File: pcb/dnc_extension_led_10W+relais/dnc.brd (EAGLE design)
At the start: 97.2 x 88 mm, 132 parts, among them IC1 LM2596S, IC2 74S244DW, Q1 IRF9321PBF, Q10 BSS316, Q11 BSS316, Q12 BSS138, Q13 BSS138, Q2 BSS670, Q3 BSS138, Q4 BSS670, Q5 BSS138, Q6 BSS670, Q7 BSS138, Q8 BSS138, Q9 BSS670, U1 MAX202CDWR, U2 74HCT595D, U3 TC7SU04F, U4 AL8807, U5 AL8807, U6 TC7SU04F

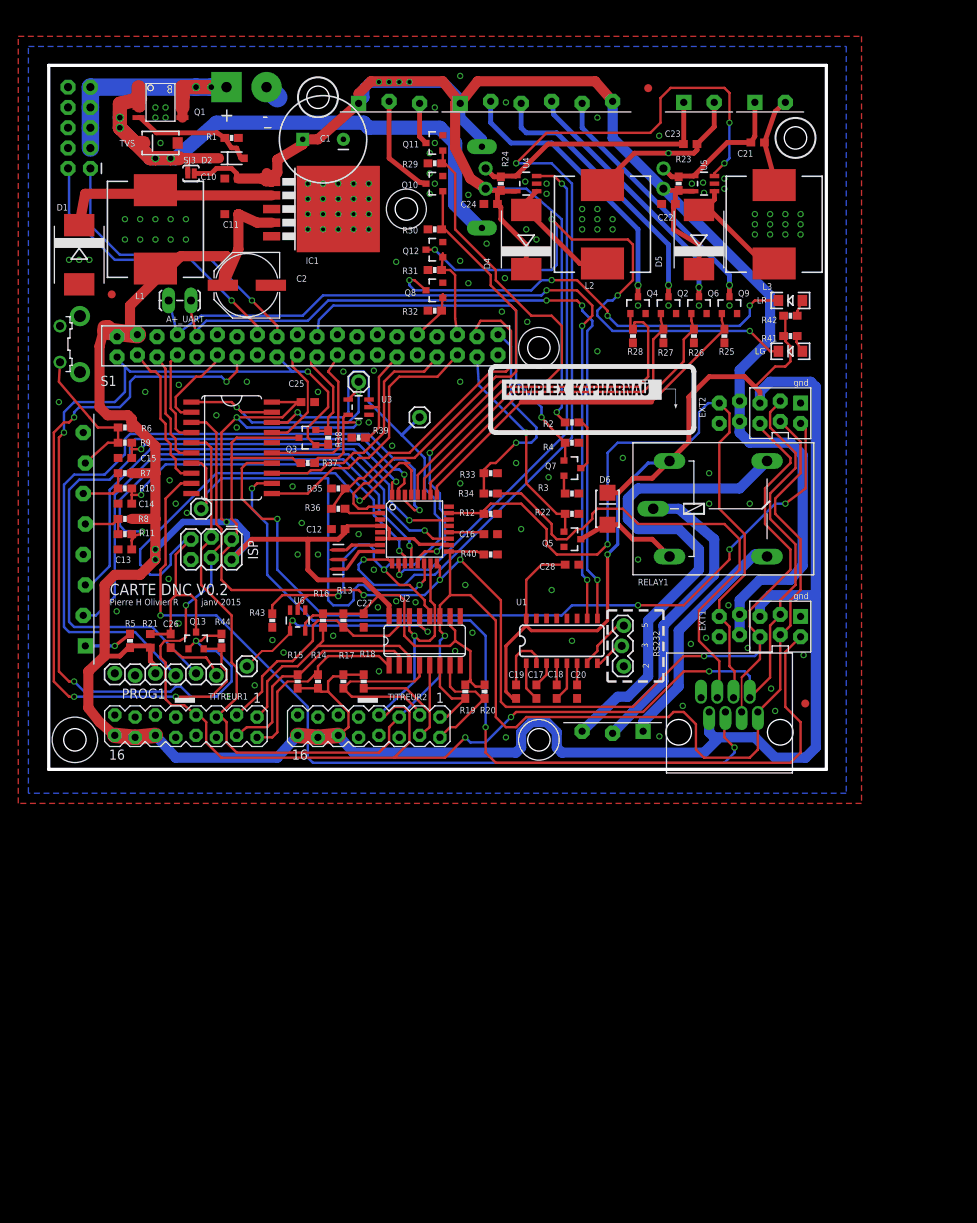
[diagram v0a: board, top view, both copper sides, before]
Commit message: add remote + enclosure
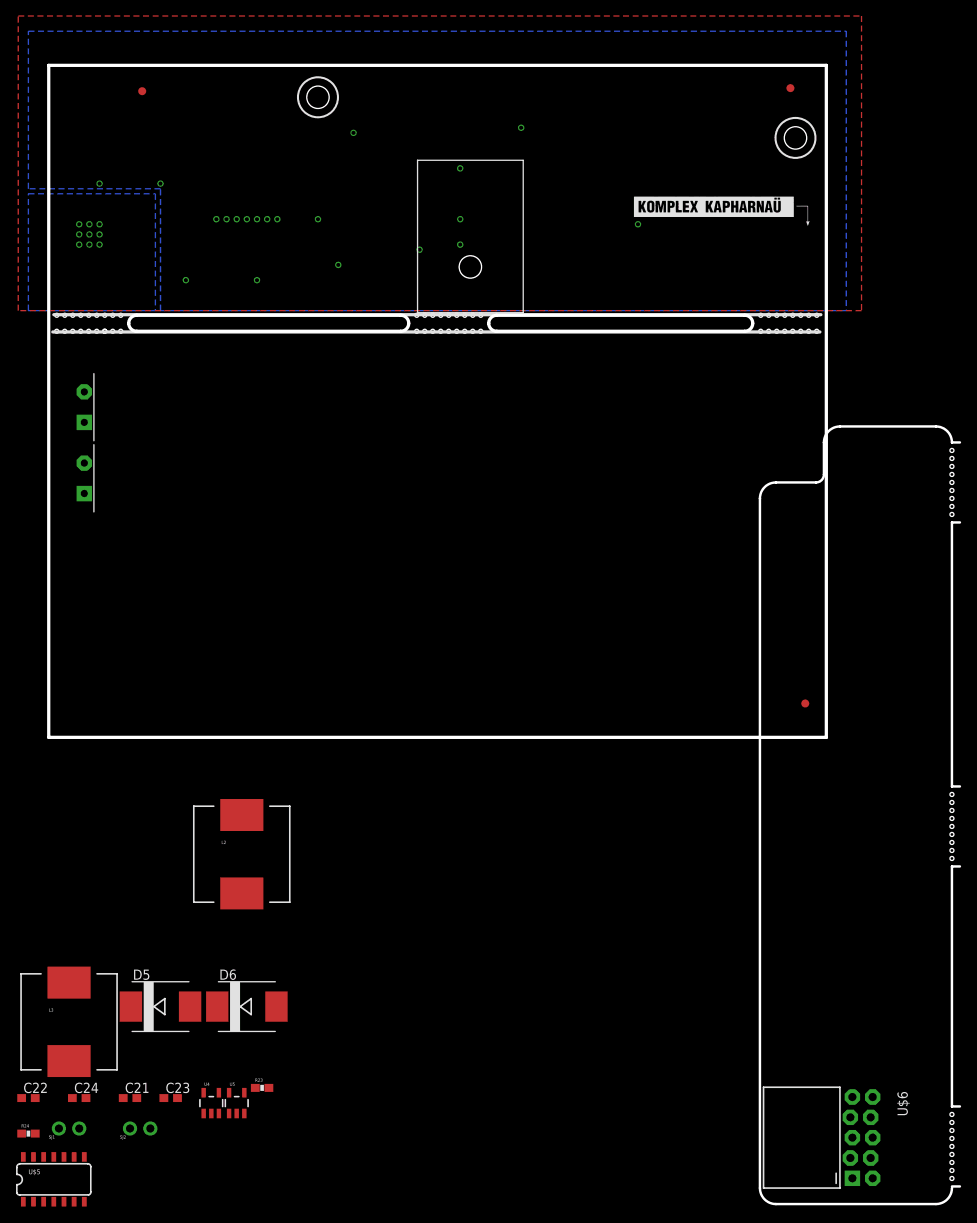
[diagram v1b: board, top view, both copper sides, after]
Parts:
- removed 16MHZ: 16MHZ, SparkFun-FreqCtrl:RESONATOR-SMD
- removed A+_UART: (no value), SparkFun:1X02_LOCK_LONGPADS
- removed AT328: ATMEGA328, SparkFun:TQFP32-08
- removed C1: 680uF30mm, SparkFun:CPOL-RADIAL-1000UF-25V
- removed C10, C11, C12, C16, C17, C18, C19, C20, C25, C26, C27, C28: 0.1uF, rcl:C0603
- removed C13, C14, C15: 1uF, rcl:C0603
- removed C2: 220u, rcl:PANASONIC_E
- removed D1, D4: 40v5A, diode:SMC
- removed D2: 10V, SparkFun-DiscreteSemi:SOD-123
- removed EXT1: EXT1, pierre_vv:EXTPINDNC
- removed EXT2: EXT2, pierre_vv:EXTPINDNC
- removed F1: 8A, SparkFun:PTC
- removed IC1: LM2596S, national-semiconductor:TO263-5
- removed IC2: 74S244DW, 74xx-us:SO20W
- removed ISP: AVR_SPI_PRG_62X3_LOCK, SparkFun:2X3_LOCK
- removed JP1: CHARGEUR, SparkFun:2X5-SHROUDED_LOCK
- removed JP2: regrck, SparkFun-Connectors:1X01
- removed JP3: atmega cs, SparkFun-Connectors:1X01
- removed JP4: allcs, SparkFun-Connectors:1X01
- removed JP5: OE 595, SparkFun-Connectors:1X01
- removed L1: 68nH3A, SparkFun:CDRH125
- removed LG, LR: (no value), SparkFun-LED:LED-1206
- removed PLUG_3.81_1: FLEX, pierre_vv:PLUG_03
- removed PLUG_3.81_2: RELAY, pierre_vv:PLUG_03
- removed PLUG_3.81_2_1: LED10W2, pierre_vv:PLUG_02
- removed PLUG_3.81_6_1: GYRO LED, pierre_vv:PLUG_06
- removed PROG1: (no value), SparkFun:1X06_LOCK
- removed Q1: IRF9321PBF, pierre_vv:SO-8
- removed Q10, Q11: BSS316, SparkFun-DiscreteSemi:SOT23-3
- removed Q12, Q13, Q3, Q5, Q7, Q8: BSS138, SparkFun-DiscreteSemi:SOT23-3
- removed Q2, Q4, Q6, Q9: BSS670, SparkFun-DiscreteSemi:SOT23-3
- removed R1, R13, R14, R15, R16, R17, R18, R19, R20, R22, R25, R26, R27, R28, R29, R30, R31, R32, R4: 100K, SparkFun-Passives:0603-RES
- removed R10, R11, R9: 33K, SparkFun-Passives:0603-RES
- removed R12: (no value), SparkFun-Passives:0603-RES
- removed R2: 100k1%, SparkFun-Passives:0603-RES
- removed R21: 10K, rcl:R0603
- removed R3: 10k1%, SparkFun-Passives:0603-RES
- removed R33, R35: 20K, SparkFun-Passives:0603-RES
- removed R34, R36, R37, R38, R39, R40, R43, R44: 10K, SparkFun-Passives:0603-RES
- removed R41, R42, R5: 1K, SparkFun-Passives:0603-RES
- removed R6, R7, R8: 56K, SparkFun-Passives:0603-RES
- removed RAW_IN: DNC_IN2PWR, pierre_vv:DNC_IN2_PWR
- removed RELAY1: G5L, relay:G5LE
- removed RS232: (no value), SparkFun-Connectors:1X03_LOCK
- removed S1: (no value), switch-omron:B3F-31XX
- removed SJ3: JUMPER-PAD-2-NC_BY_PASTE, SparkFun-Passives:PAD-JUMPER-2-NC_BY_PASTE_YES_SILK
- removed TITREUR1, TITREUR2: DNC_TITREUR, pierre_vv:DNC_TITREUR
- removed TVS: TVS-30V, SparkFun:SMA-DIODE
- removed U$4: RASPIA+, pierre_vv:RASPIA+
- removed U$8: RJ45-EXTDNC, con-amphenol-rj45-ld:RJ45-TRAFO
- removed U1: MAX202CDWR, SparkFun-DigitalIC:SO016
- removed U2: 74HCT595D, IC:SO16
- removed U3, U6: TC7SU04F, SparkFun-DigitalIC:SOT23-5
- added PLUG_3.81_2_3: LED10W1, pierre_vv:PLUG_02
- added U$5: ATTINY84, SparkFun-DigitalIC:SO14
- D6: value (none) -> 40v5A; device SparkFun-DiscreteSemi:SMA-DIODE_ALT -> diode:SMC
- PLUG_3.81_2_2: value LED10W1 -> LED10W2
- U$6: value M08 -> (none); device pierre_vv:PLUG_08 -> pierre_vv:2X5_RIGHTANGLEDNC
- moved C21 142.9 mm to (10.2, -45.1)
- moved C22 137.4 mm to (-2.54, -45.1), turned to 0 degrees
- moved C23 135.8 mm to (15.2, -45.1)
- moved SJ2 135.6 mm to (11.4, -48.9), turned to 0 degrees
- moved L3 133.1 mm to (2.54, -35.6), turned to 0 degrees
- moved R24 132.6 mm to (-2.54, -49.5), turned to 0 degrees
- moved SJ1 129.7 mm to (2.54, -48.9), turned to 0 degrees
- moved U5 128.9 mm to (23.5, -45.7), turned to 0 degrees
- moved R23 124.4 mm to (26.7, -43.8), turned to 0 degrees
- moved C24 123.0 mm to (3.81, -45.1), turned to 0 degrees
- moved U4 121.5 mm to (20.3, -45.7), turned to 0 degrees
- moved D5 117.2 mm to (14.0, -33.7), turned to 0 degrees
- moved PLUG_3.81_2_2 97.8 mm to (4.45, 32.4), turned to 90 degrees
- moved L2 90.7 mm to (24.1, -14.6), turned to 0 degrees
- moved U$6 85.6 mm to (88.9, 38.9), turned to 270 degrees
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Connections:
- removed net +3V3: Q13.1, Q3.1, R38.2, R44.2, U$4.1, U$4.17
- removed net +5V: AT328.18, AT328.4, AT328.6, C11.1, C12.1, C19.1, C2.+, C25.1, C27.1, C28.1, D6.C, EXT1.5V, EXT2.5V, IC1.4, IC2.20, ISP.2, L1.2, PROG1.4, R13.2, R14.2, R15.2, R16.2, R17.2, R18.2, R19.2, R20.2, R21.2, R37.2, R41.2, R42.2, R5.2, R6.2, R7.2, R8.2, RELAY1.2, TITREUR1.12, TITREUR1.14, TITREUR1.16, TITREUR2.12, TITREUR2.14, TITREUR2.16, U$4.2, U$4.4, U$8.1, U1.16, U2.10, U2.16, U3.5, U6.5
- removed net /REG_RCK_5V=ACTIVE_CS: JP5.1, U2.13, U6.4
- removed net ALL_CS_ENABLE_ACTIVE_LOW_5V: IC2.1, IC2.19, JP4.1, U3.4
- removed net ANALOG_BAT: AT328.24
- removed net ANALOG_RAW: Q7.2, R3.2
- removed net AREF: AT328.20, C16.1
- removed net ATMEGA_CS: IC2.13, U$4.33
- removed net ATMEGA_CS_5V: AT328.14, IC2.7, JP3.1
- removed net CHARGING: JP1.2, U$4.16
- removed net CODE: AT328.23, EXT1.RETOURANALOG, EXT2.RETOURANALOG, R12.1, U$8.6
- removed net CS_TRIGGER_ACTIVE_HIGH: R39.2, U$4.29, U3.2
- removed net DTR: C26.1, PROG1.1
- removed net EXT1_CS: IC2.8, U$4.3
- removed net EXT1_CS_5V: EXT1./CS, IC2.12
- removed net EXT2_CS: IC2.6, U$4.5
- removed net EXT2_CS_5V: EXT2./CS, IC2.14
- removed net EXT3_CS: IC2.4, U$4.7
- removed net EXT3_CS_5V: IC2.16
- removed net FLOAT1: AT328.19, U$6.2
- removed net FLOAT2: AT328.22, U$6.3
- removed net GYRO_1: AT328.28, Q4.1, R28.2
- removed net GYRO_2: AT328.27, Q2.1, R27.2
- removed net GYRO_3: AT328.26, Q6.1, R26.2
- removed net GYRO_4: AT328.25, Q9.1, R25.2
- removed net INT_ATMEGA: R35.2, R36.1, U$4.38
- removed net INT_ATMEGA_5V: AT328.2, R36.2
- removed net INT_TELECO: R33.2, R34.1, U$4.40
- removed net INT_TELECO_5V: R34.2, U$8.4
- removed net LEDR: LR.C, Q8.3
- removed net LED_G: Q12.1, R31.2, U$4.36
- removed net LED_R: Q8.1, R32.2, U$4.32
- removed net LG: LG.C, Q12.3
- removed net MISO: Q3.2, R38.1, U$4.21
- removed net MISO_5V: AT328.16, EXT1.MISO, EXT2.MISO, ISP.1, Q3.3, R37.1, U$8.5
- removed net MOSI: IC2.17, U$4.19
- removed net MOSI_5V: AT328.15, EXT1.MOSI, EXT2.MOSI, IC2.3, ISP.4, TITREUR1.7, TITREUR2.7, U$8.8, U2.14
- removed net N$1: D1.C, IC1.2, L1.1
- removed net N$10: PLUG_3.81_6_1.2, Q4.3
- removed net N$11: PLUG_3.81_6_1.3, Q2.3
- removed net N$12: PLUG_3.81_6_1.4, Q6.3
- removed net N$13: PLUG_3.81_6_1.5, Q9.3
- removed net N$14: PLUG_3.81_1.2, Q10.3
- removed net N$15: PLUG_3.81_2.3, RELAY1.O
- removed net N$16: D6.A, Q5.3, RELAY1.1
- removed net N$18: LG.A, R41.1
- removed net N$20: R10.1, R7.1, U$6.6
- removed net N$21: LR.A, R42.1
- removed net N$24: C19.2, U1.2
- removed net N$25: R5.1, U$6.1
- removed net N$3: Q7.3, R2.1
- removed net N$35: C20.1, U1.6
- removed net N$4: PLUG_3.81_2.1, RELAY1.S
- removed net N$43: 16MHZ.1, AT328.7
- removed net N$44: 16MHZ.3, AT328.8
- removed net N$50: C18.2, U1.5
- removed net N$51: C18.1, U1.4
- removed net N$52: C17.2, U1.3
- removed net N$53: C17.1, U1.1
- removed net N$6: D4.A, L2.1, U4.1
- removed net N$7: D5.A, L3.1, U5.1
- removed net N$8: PLUG_3.81_2.2, RELAY1.P
- removed net N$9: PLUG_3.81_1.3, Q11.3
- removed net PROTECT_GATE: D2.A, Q1.4, R1.1
- removed net PRXD_PIN2_RS232: RS232.1, U1.7
- removed net PTXD_PIN3_RS232: RS232.2, U1.8
- removed net PUSH1: AT328.32, C15.1, R9.2
- removed net PUSH2: AT328.11, C14.1, R10.2
- removed net PUSH3: AT328.12, C13.1, R11.2
- removed net PWM_FLEX_1: AT328.1, Q10.1, R30.2
- removed net PWM_FLEX_2: AT328.13, Q11.1, R29.2
- removed net RAW_POL_PROTECTED: D2.C, F1.P$1MOV, Q1.1, Q1.2, Q1.3, SJ3.1, TVS.C
- removed net RAW_UNPROTECTED: JP1.3, JP1.5, JP1.7, JP1.9, Q1.5, Q1.6, Q1.7, Q1.8, RAW_IN.1
- removed net READ_BATTERY: Q7.1, R4.2, U$4.22
- removed net REG_RCK: IC2.2, U$4.11
- removed net REG_RCK_5V: IC2.18, JP2.1, R43.2, U2.12, U6.2
- removed net RELAY1: Q5.1, R22.2, U$4.37
- removed net RELAY_CHARGE_BOARD: JP1.1, U$4.18
- removed net RESET: Q13.2, R44.1, U$4.13
- removed net RESET_5V: AT328.29, C26.2, ISP.5, Q13.3, R21.1
- removed net RST1: R16.1, TITREUR1.1, U2.3
- removed net RST2: R14.1, TITREUR1.2, U2.1
- removed net RST3: R13.1, TITREUR1.3, U2.15
- removed net RST4: R15.1, TITREUR1.4, U2.2
- removed net RST5: R19.1, TITREUR2.1, U2.6
- removed net RST6: R20.1, TITREUR2.2, U2.7
- removed net RST7: R17.1, TITREUR2.3, U2.4
- removed net RST8: R18.1, TITREUR2.4, U2.5
- removed net RX-I: AT328.30, PROG1.3
- removed net RXA+: A+_UART.2, U$4.10, U1.9
- removed net SCK: IC2.15, U$4.23
- removed net SCK_5V: AT328.17, EXT1.SCK, EXT2.SCK, IC2.5, ISP.3, R40.2, TITREUR1.5, TITREUR2.5, U$8.7, U2.11
- removed net TELECO_CS: IC2.11, U$4.35
- removed net TELECO_CS_5V: IC2.9, U$8.3
- removed net TX-O: AT328.31, PROG1.2
- removed net TXA+: A+_UART.1, U$4.8, U1.10
- net GND: no longer 16MHZ.2, AT328.21, AT328.3, AT328.5, C1.2, C10.2, C11.2, C12.2, C13.2, C14.2, C15.2, C16.2, C2.-, C20.2, C25.2, C27.2, C28.2, D1.A, EXT1.1_GND, EXT1.GND2, EXT2.1_GND, EXT2.GND2, IC1.3, IC1.5, IC1.THERMAL, IC2.10, ISP.6, JP1.10, JP1.4, JP1.6, JP1.8, PROG1.5, PROG1.6, Q10.2, Q11.2, Q12.2, Q2.2, Q4.2, Q5.2, Q6.2, Q8.2, Q9.2, R1.2, R12.2, R22.1, R25.1, R26.1, R27.1, R28.1, R29.1, R3.1, R30.1, R31.1, R32.1, R33.1, R35.1, R39.1, R4.1, R40.1, R43.1, RAW_IN.2, RS232.3, S1.1, TITREUR1.11, TITREUR1.13, TITREUR1.15, TITREUR1.8, TITREUR2.11, TITREUR2.13, TITREUR2.15, TITREUR2.8, TVS.A, U$4.14, U$4.20, U$4.25, U$4.30, U$4.34, U$4.39, U$4.6, U$4.9, U$6.4, U$6.8, U$8.2, U1.15, U2.8, U3.3, U6.3
- net LED+1: now also PLUG_3.81_2_2.1; no longer PLUG_3.81_2_1.1
- net LED+2: now also PLUG_3.81_2_3.1; no longer PLUG_3.81_2_2.1
- net LED-1: now also PLUG_3.81_2_2.2; no longer PLUG_3.81_2_1.2
- net LED-2: now also PLUG_3.81_2_3.2; no longer PLUG_3.81_2_2.2
- net N$22: now also D5.A, L2.1, U4.1; no longer R6.1, R9.1, S1.2, U$6.7
- net N$23: now also D6.A, L3.1, U5.1; no longer R11.1, R8.1, U$6.5
- net PWM_LED_1: no longer AT328.9
- net PWM_LED_2: no longer AT328.10
- net RAW_FUSED: now also D6.C; no longer C1.1, C10.1, D4.C, EXT1.RAW, EXT1.RAW2, EXT2.RAW, EXT2.RAW2, F1.P$2, IC1.1, PLUG_3.81_1.1, PLUG_3.81_6_1.1, PLUG_3.81_6_1.6, R2.2, SJ3.2
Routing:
- net +5V: track 568.4 -> 0.00 mm, vias 6 -> 0
- net RAW_FUSED: track 262.9 -> 0.00 mm, vias 5 -> 0
- net MOSI_5V: track 209.3 -> 0.00 mm, vias 5 -> 0
- net SCK_5V: track 202.2 -> 0.00 mm, vias 1 -> 0
- net MISO_5V: track 171.6 -> 0.00 mm, vias 4 -> 0
- net PWM_LED_1: track 124.0 -> 0.00 mm, vias 4 -> 0
- net +3V3: track 123.9 -> 0.00 mm, vias 4 -> 0
- net EXT1_CS_5V: track 115.9 -> 0.00 mm, vias 2 -> 0
- net TELECO_CS_5V: track 108.2 -> 0.00 mm, vias 2 -> 0
- net EXT2_CS_5V: track 103.6 -> 0.00 mm, vias 4 -> 0
- net TXA+: track 99.1 -> 0.00 mm, vias 3 -> 0
- net RXA+: track 96.1 -> 0.00 mm, vias 3 -> 0
- net CODE: track 95.7 -> 0.00 mm, vias 1 -> 0
- net RX-I: track 92.2 -> 0.00 mm, vias 1 -> 0
- net RESET: track 90.9 -> 0.00 mm, vias 4 -> 0
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- added copper zone on layer 16, net SYSTEM_LOAD
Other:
- board size 97.2 x 88 mm -> 97.2 x 84 mm
- board text added: "BATT+"
- board text added: "DNC carte batterie V0"
- board text added: "GND"
- board text added: "Pierre H Olivier R Jan 2015"
- board text added: "Relay -"
- board text added: "SUPPLY"
- board text removed: "2"
- board text removed: "3"
- board text removed: "5"
- board text removed: "BRD+10mm"
- board text removed: "BRD+13,5mm"
- board text removed: "BRD+7,1mm diam4mm"
- board text removed: "BRD+8mm"
- board text removed: "CARTE DNC V0.2"
- board text removed: "Pierre H Olivier R"
- board text removed: "RPI+3mm"
- board text removed: "RPI+3mm diam15mm"
- board text removed: "RPI+6mm"
- board text removed: "RPI+7mm"
- board text removed: "RPI-2mm"
- board text removed: "janv 2015"
